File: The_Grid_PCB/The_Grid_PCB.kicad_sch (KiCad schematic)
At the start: 60 parts, among them J1 TC2050, J2 Screw_Terminal_01x02, J3 Conn_01x02, J4 Conn_01x02, J5 Screw_Terminal_01x02, J6 Screw_Terminal_01x02, J7 Screw_Terminal_01x02, J8 Screw_Terminal_01x02, J9 Screw_Terminal_01x02, U1 STM32F030C8Tx, U2 SN65HVD11HD, U3 TPS54331DR, X1 X322516MLB4SI

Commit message: update wiring diagram again sob
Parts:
- removed C19, C20: 100uF, PCM_JLCPCB:C_1206, symbol PCM_JLCPCB-Capacitors:1206,100uF
- removed R11: 43kΩ, PCM_JLCPCB:R_0603, symbol PCM_JLCPCB-Resistors:0603,43kΩ
- removed R14: 3kΩ, PCM_JLCPCB:R_0603, symbol PCM_JLCPCB-Resistors:0603,3kΩ
- removed R15: 240Ω, PCM_JLCPCB:R_0603, symbol PCM_JLCPCB-Resistors:0603,240Ω
- removed R6: 10Ω, PCM_JLCPCB:R_0603, symbol PCM_JLCPCB-Resistors:0603,10Ω
- removed U2: SN65HVD11HD, Package_SO:SOIC-8_3.9x4.9mm_P1.27mm, symbol Interface_UART:SN65HVD11HD
- added C19: 10uF, PCM_JLCPCB:C_0603, symbol PCM_JLCPCB-Capacitors:0603,10uF
- added C20, C21: 47uF, PCM_JLCPCB:C_1206, symbol PCM_JLCPCB-Capacitors:1206,47uF
- added C22: 22uF, PCM_JLCPCB:C_0603, symbol PCM_JLCPCB-Capacitors:0603,22uF
- added C24: 100nF, PCM_JLCPCB:C_0805, symbol PCM_JLCPCB-Capacitors:0805,100nF
- added D2: LED, PCM_JLCPCB:D_0603, symbol Device:LED
- added R12: 68kΩ, PCM_JLCPCB:R_0603, symbol PCM_JLCPCB-Resistors:0603,68kΩ
- added R15: 200Ω, PCM_JLCPCB:R_0603, symbol PCM_JLCPCB-Resistors:0603,200Ω
- added R16: 560Ω, PCM_JLCPCB:R_0603, symbol PCM_JLCPCB-Resistors:0603,560Ω
- added R17: 1.2kΩ, PCM_JLCPCB:R_0603, symbol PCM_JLCPCB-Resistors:0603,1.2kΩ
- added R2: 1.5kΩ, PCM_JLCPCB:R_0603, symbol PCM_JLCPCB-Resistors:0603,1.5kΩ
- added R7: 10Ω, PCM_JLCPCB:R_0603, symbol PCM_JLCPCB-Resistors:0603,10Ω
- added U2: SN65HVD485EDR, Package_SO:SOIC-8_3.9x4.9mm_P1.27mm, symbol SN65HVD485EDR:SN65HVD485EDR
- added U4: AMS1117-3.3, Package_TO_SOT_SMD:SOT-223-3_TabPin2, symbol Regulator_Linear:AMS1117-3.3
- J1: footprint Connector:Tag-Connect_TC2070-IDC-FP_2x07_P1.27mm_Vertical -> Connector:Tag-Connect_TC2050-IDC-FP_2x05_P1.27mm_Vertical; now fitted
- L1: value 6.8uH -> 8.2uH; footprint Inductor_SMD:L_Sumida_CDMC6D28_7.25x6.5mm -> Inductor_SMD:L_Bourns_SRP7028A_7.3x6.6mm; LCSC C5189749 -> C167222
- renumbered C21 to C23, C22 to C25, D2 to D3, D3 to D4, R9 to R10, R10 to R11, R12 to R13, R13 to R14, R16 to R18, R17 to R19, R2 to R3, R3 to R4, R4 to R5, R5 to R6, R7 to R8, R8 to R9
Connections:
- net +24V: now also D2.2 (A)
- net +3.3V: now also C22.1, C24.1, U4.2 (VO); no longer C10.1, C23.1, C25.1, L1.2, R13.1, R5.1
- net DE: now also U2.2 (~{RE}), U2.3 (DE)
- net GND: now also C19.2, C20.1, C21.1, C22.2, C24.2, R17.2, R2.2, U2.5 (GND), U4.1 (GND)
- net RSB: now also R7.2
- net RX: now also U2.1 (R)
- net TX: now also U2.4 (D)
- net at R8.1: now also U2.6 (A)
- net at R14.2, U3.5 (VSENSE): now also R15.1
- net at C18.1, U3.6 (COMP): now also R12.1
- net at C17.1: now also R12.2
- new net: R15.2, R16.1
- new net: R16.2, R17.1
- new net: D2.1 (K), R2.1
- new net: R7.1, U2.7 (B)
- new net +5V: C10.1, C19.1, C20.2, C21.2, C23.1, C25.1, L1.2, R13.1, R5.1, U2.8 (VCC), U4.3 (VI)
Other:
- note added: "1.96k"
- note added: "24V Power indication LED"
- note added: "3V3 LDO"
- note added: "3V3 Power indication LED"
- note added: "5V Buck"
- note removed: "3.24k"
- note removed: "Power"
- note removed: "Power indication LED"
- moved on the sheet: R5, R8

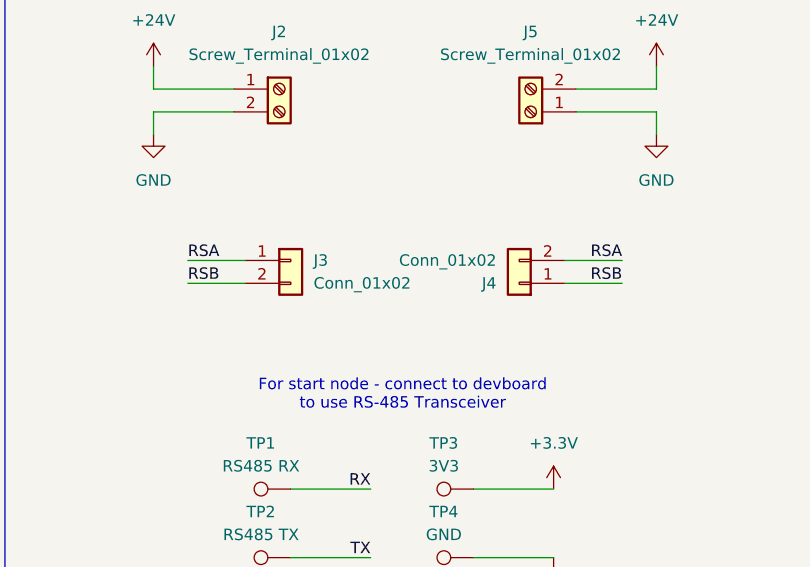
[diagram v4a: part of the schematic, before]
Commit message: revised pcb nevin/miguel feedback
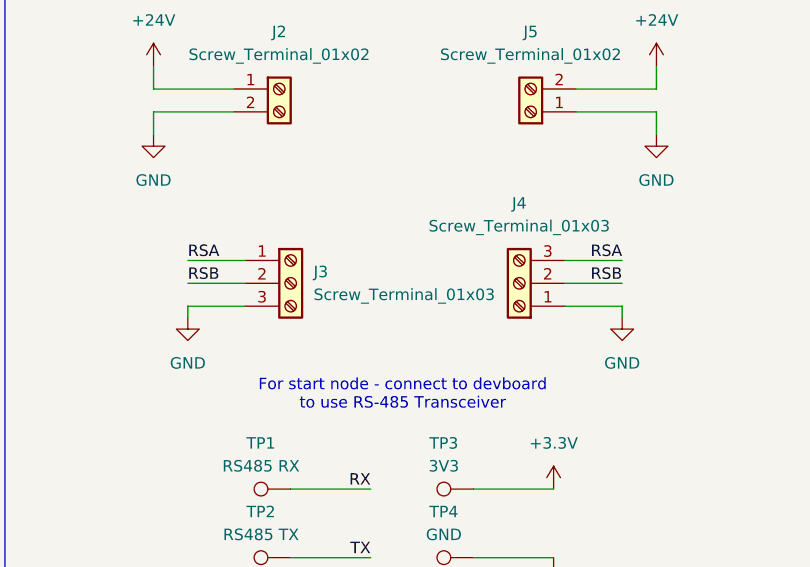
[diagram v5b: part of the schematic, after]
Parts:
- removed J3, J4: Conn_01x02, james_custom_footprint_library:JST_XH_B02B-XH-A_02x2.50mm_7.32x7.5_RightAngle, symbol Connector_Generic:Conn_01x02
- added J3, J4: Screw_Terminal_01x03, TerminalBlock:TerminalBlock_Xinya_XY308-2.54-3P_1x03_P2.54mm_Horizontal, symbol Connector:Screw_Terminal_01x03
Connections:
- net GND: now also J3.3 (Pin_3), J4.1 (Pin_1)
- net RSA: now also J3.1 (Pin_1), J4.3 (Pin_3)
- net RSB: now also J3.2 (Pin_2), J4.2 (Pin_2)

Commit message: rev1 pcb sent to prod
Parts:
- removed C1: 1uF, PCM_JLCPCB:C_0603, symbol PCM_JLCPCB-Capacitors:0603,1uF
- removed C19: 10uF, PCM_JLCPCB:C_0603, symbol PCM_JLCPCB-Capacitors:0603,10uF
- removed C2: 10nF, PCM_JLCPCB:C_0603, symbol PCM_JLCPCB-Capacitors:0603,10nF
- removed C22: 22uF, PCM_JLCPCB:C_0603, symbol PCM_JLCPCB-Capacitors:0603,22uF
- removed C24: 100nF, PCM_JLCPCB:C_0805, symbol PCM_JLCPCB-Capacitors:0805,100nF
- removed C3, C4: 18pF, PCM_JLCPCB:C_0603, symbol PCM_JLCPCB-Capacitors:0603,18pF
- removed C5: 4.7uF, PCM_JLCPCB:C_0603, symbol PCM_JLCPCB-Capacitors:0603,4.7uF
- removed C6, C7, C8: 100nF, PCM_JLCPCB:C_0603, symbol PCM_JLCPCB-Capacitors:0603,100nF
- removed J1: TC2050, Connector:Tag-Connect_TC2050-IDC-FP_2x05_P1.27mm_Vertical, symbol Connector:TC2050
- removed R3: 330Ω, PCM_JLCPCB:R_0603, symbol PCM_JLCPCB-Resistors:0603,330Ω
- removed R4: 10kΩ, PCM_JLCPCB:R_0603, symbol PCM_JLCPCB-Resistors:0603,10kΩ
- removed U1: STM32F030C8Tx, Package_QFP:LQFP-48_7x7mm_P0.5mm, symbol MCU_ST_STM32F0:STM32F030C8Tx
- removed U4: AMS1117-3.3, Package_TO_SOT_SMD:SOT-223-3_TabPin2, symbol Regulator_Linear:AMS1117-3.3
- removed X1: X322516MLB4SI, PCM_JLCPCB:OSC-SMD_4P-L3.2-W2.5-BL, symbol PCM_JLCPCB-Crystals:Crystal, 16MHz, 9pF
- added TP5: 5V, TestPoint:TestPoint_THTPad_D2.0mm_Drill1.0mm, symbol Connector:TestPoint
- added U1: STM32 Blue Pill, BluePill_Header:STM32BluePill, symbol BluePill_Header:STM32_BluePill
- J2: renamed from J3; LCSC C918121 -> C5188443
- J3: renamed from J4; LCSC C918121 -> C5188443
- renumbered C9 to C1, C18 to C10, C20 to C11, C21 to C12, C23 to C13, C25 to C14, C10 to C2, C11 to C3, C12 to C4, C13 to C5, C14 to C6, C15 to C7, C16 to C8, C17 to C9, J2 to J1, J5 to J4, J6 to J5, J7 to J6, J8 to J7, J9 to J8, R12 to R10, R13 to R11, R14 to R12, R15 to R13, R16 to R14, R17 to R15, R18 to R16, R19 to R17, R5 to R3, R6 to R4, R7 to R5, R8 to R6, R9 to R7, R10 to R8, R11 to R9
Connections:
- net +3.3V: now also U1.1 (VBAT), U1.18 (3V3), U1.40 (3V3)
- net +5V: now also TP5.1, U1.38 (5V)
- net B1: now also U1.12 (PA7)
- net B2: now also U1.35 (PB7)
- net B3: now also U1.5 (PA0)
- net B4: now also U1.8 (PA3)
- net DE: now also U1.9 (PA4)
- net G1: now also U1.13 (PB0)
- net G2: now also U1.34 (PB6)
- net G3: now also U1.6 (PA1)
- net G4: now also U1.37 (PB9)
- net GND: now also U1.19 (GND), U1.20 (GND), U1.39 (GND)
- net Microswitch1: now also U1.30 (PA15)
- net Microswitch2: now also U1.31 (PB3)
- net Microswitch3: now also U1.32 (PB4)
- net Microswitch4: now also U1.33 (PB5)
- net R1: now also U1.14 (PB1)
- net R2: now also U1.11 (PA6)
- net R3: now also U1.7 (PA2)
- net R4: now also U1.36 (PB8)
- net RX: now also U1.16 (PB11)
- net TX: now also U1.15 (PB10)
- no-connect marks 18 -> 15
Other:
- note added: "PB1 -> TIM3_CH4 (R1) PB0 -> TIM3_CH3 (G1) PA7 -> TIM3_CH2 (B1) PA6 -> TIM3_CH1 (R2) PB6 -> TIM4_CH1 (G2) PB7 -> TIM4_CH2 (B2) PA2 -> TIM2_CH3 (R3) PA1 -> TIM2_CH2 (G3) PA0 -> TIM2_CH1 (B3) PB8 -> TIM4_CH3 (R4) PB9 -> TIM4_CH4 (G4) PA3 -> TIM2_CH4 (B4)"
- note removed: "3V3 LDO"
- note removed: "PB8 -> TIM16_CH1 (R1) PB9 -> TIM17_CH1 (G1) PA3 -> TIM15_CH2 (B1) PA4 -> TIM14_CH1 (R2) PA6 -> TIM3_CH1 (G2) PA7 -> TIM3_CH2 (B2) PA8 -> TIM1_CH1 (R3) PA10 -> TIM1_CH3 (G3) PA11 -> TIM1_CH4 (B3) PB0 -> TIM3_CH3 (R4) PB1 -> TIM3_CH4 (G4) PB14 -> TIM15_CH1 (B4)"
- moved on the sheet: D1, D2, R1, R2, TP1, TP2, TP3, TP4
